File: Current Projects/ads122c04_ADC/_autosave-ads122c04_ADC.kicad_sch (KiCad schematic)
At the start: 23 parts, among them J1 Conn_01x05, J2 Conn_01x04, U1 ADS122C04IPWR, U2 MCP1711T-33I/OT

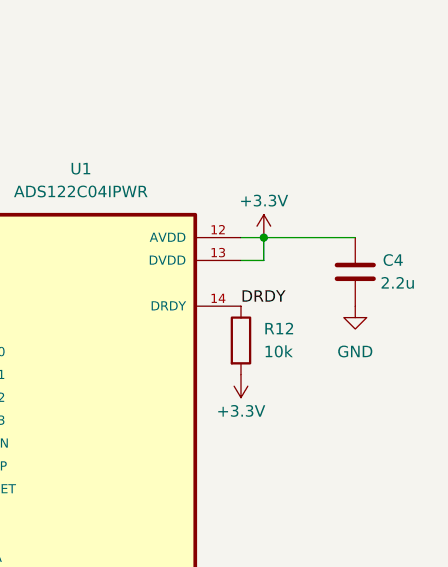
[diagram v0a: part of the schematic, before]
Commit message: ADC board with changes from Jacobs review.
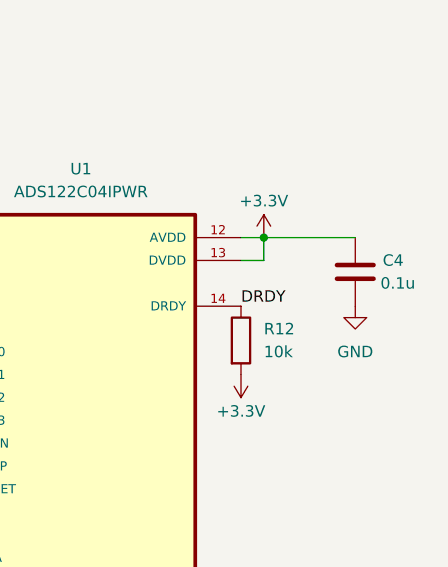
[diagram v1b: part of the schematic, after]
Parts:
- C4: value 2.2u -> 0.1u
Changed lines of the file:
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@@
 			)
 		)
-		(property "Value" "2.2u"
+		(property "Value" "0.1u"
 			(at 195.834 76.2 0)
 			(effects

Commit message: Added BOM to project. See the csv file.
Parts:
- R1, R2, R3, R4, R5, R6, R7, R8: now left out of the parts list
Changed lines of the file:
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@@
 		(unit 1)
 		(exclude_from_sim no)
-		(in_bom yes)
+		(in_bom no)
 		(on_board yes)
 		(dnp no)
@@
 		(unit 1)
 		(exclude_from_sim no)
-		(in_bom yes)
+		(in_bom no)
 		(on_board yes)
 		(dnp no)
@@
 		(unit 1)
 		(exclude_from_sim no)
-		(in_bom yes)
+		(in_bom no)
 		(on_board yes)
 		(dnp no)
@@
 		(unit 1)
 		(exclude_from_sim no)
-		(in_bom yes)
+		(in_bom no)
 		(on_board yes)
 		(dnp no)
@@
 		(unit 1)
 		(exclude_from_sim no)
-		(in_bom yes)
+		(in_bom no)
 		(on_board yes)
 		(dnp no)
@@
 		(unit 1)
 		(exclude_from_sim no)
-		(in_bom yes)
+		(in_bom no)
 		(on_board yes)
 		(dnp no)
@@
 		(unit 1)
 		(exclude_from_sim no)
-		(in_bom yes)
+		(in_bom no)
 		(on_board yes)
 		(dnp no)
@@
 		(unit 1)
 		(exclude_from_sim no)
-		(in_bom yes)
-		(on_board yes)
-		(dnp no)
+		(in_bom no)
+		(on_board yes)
+		(dnp no)
